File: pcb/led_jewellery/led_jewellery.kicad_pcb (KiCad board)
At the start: 2 copper layers, 12.3 x 27.2 mm, 6 parts, among them J1 Conn_01x01, J2 Conn_01x01, SW1 SW_SPST

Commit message: update pcb
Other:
- board size 12.3 x 27.2 mm -> 12.3 x 25.6 mm
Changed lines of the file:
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@@
 		(grid_origin 124.5 72)
 		(pcbplotparams
-			(layerselection 0x00000000_00000000_55555555_575555ff)
+			(layerselection 0x00000000_00000000_55555555_5755557f)
 			(plot_on_all_layers_selection 0x00000000_00000000_00000000_00000000)
 			(disableapertmacros no)
@@
 			)
 		)
+		(property "LCSC_part#" ""
+			(at 0 0 225)
+			(unlocked yes)
+			(layer "F.Fab")
+			(hide yes)
+			(effects
+				(font
+					(size 1 1)
+					(thickness 0.15)
+				)
+			)
+		)
 		(property ki_fp_filters "LED* LED_SMD:* LED_THT:*")
 		(sheetname "/")
 		(sheetfile "led_jewellery.kicad_sch")
-		(attr smd)
+		(attr smd dnp)
 		(fp_line
 			(start 1.6 1)
@@
 			(at -3.2 0 225)
 			(size 5.5 1)
-			(layers "F.Cu" "F.Mask" "F.Paste")
+			(layers "F.Cu" "F.Mask")
 			(net 3 "/BAT-")
 			(pinfunction "K")
@@
 			(at 3.2 0 225)
 			(size 5.5 1)
-			(layers "F.Cu" "F.Mask" "F.Paste")
+			(layers "F.Cu" "F.Mask")
 			(net 2 "/LED+")
 			(pinfunction "A")
@@
 			)
 		)
+		(property "LCSC_part#" "C17408"
+			(at 0 0 180)
+			(unlocked yes)
+			(layer "F.Fab")
+			(hide yes)
+			(effects
+				(font
+					(size 1 1)
+					(thickness 0.15)
+				)
+			)
+		)
 		(property ki_fp_filters "R_*")
 		(sheetname "/")
@@
 		)
 		(property "Description" "Single Pole Single Throw (SPST) switch"
+			(at 0 0 0)
+			(unlocked yes)
+			(layer "F.Fab")
+			(hide yes)
+			(effects
+				(font
+					(size 1 1)
+					(thickness 0.15)
+				)
+			)
+		)
+		(property "LCSC_part#" "C501583"
 			(at 0 0 0)
 			(unlocked yes)
@@
 			(unlocked yes)
 			(layer "B.SilkS")
+			(hide yes)
 			(effects
 				(font
@@
 		(property "Description" "Generic connector, single row, 01x01, script generated (kicad-library-utils/schlib/autogen/connector/)"
 			(at 0 0 45)
+			(unlocked yes)
+			(layer "B.Fab")
+			(hide yes)
+			(effects
+				(font
+					(size 1 1)
+					(thickness 0.15)
+				)
+				(justify mirror)
+			)
+		)
+		(property "LCSC_part#" ""
+			(at 0 0 225)
 			(unlocked yes)
 			(layer "B.Fab")
@@
 		(sheetname "/")
 		(sheetfile "led_jewellery.kicad_sch")
-		(attr smd)
+		(attr smd dnp)
 		(fp_text user "${REFERENCE}"
 			(at 0 -6.999999 45)
@@
 			(at 0 0 225)
 			(size 9 9)
-			(layers "B.Cu" "B.Mask" "B.Paste")
+			(layers "B.Cu" "B.Mask")
 			(net 3 "/BAT-")
 			(pinfunction "Pin_1")
@@
 			(unlocked yes)
 			(layer "B.SilkS")
+			(hide yes)
 			(effects
 				(font
@@
 		(property "Description" "Generic connector, single row, 01x01, script generated (kicad-library-utils/schlib/autogen/connector/)"
 			(at 0 0 0)
+			(unlocked yes)
+			(layer "B.Fab")
+			(hide yes)
+			(effects
+				(font
+					(size 1 1)
+					(thickness 0.15)
+				)
+				(justify mirror)
+			)
+		)
+		(property "LCSC_part#" ""
+			(at 0 0 180)
 			(unlocked yes)
 			(layer "B.Fab")
@@
 		(sheetname "/")
 		(sheetfile "led_jewellery.kicad_sch")
-		(attr smd)
+		(attr smd dnp)
 		(fp_text user "${REFERENCE}"
 			(at 0 -7 0)
@@
 			(at 0 0 180)
 			(size 9 9)
-			(layers "B.Cu" "B.Mask" "B.Paste")
+			(layers "B.Cu" "B.Mask")
 			(net 4 "/BAT+")
 			(pinfunction "Pin_1")
@@
 	)
 	(gr_arc
-		(start 120.952656 90.468665)
-		(mid 118.826176 90.473825)
-		(end 118.831189 88.347491)
-		(stroke
-			(width 0.05)
-			(type default)
-		)
-		(layer "Edge.Cuts")
-	)
-	(gr_arc
 		(start 127.115338 79.4)
 		(mid 127.339014 79.51417)
@@
 		(layer "Edge.Cuts")
 	)
+	(gr_arc
+		(start 124.5 65.573)
+		(mid 125.304105 65.623501)
+		(end 126.095573 65.774209)
+		(stroke
+			(width 0.05)
+			(type default)
+		)
+		(layer "Edge.Cuts")
+	)
 	(gr_line
 		(start 120.952656 90.468665)
@@
 			(width 0.05)
 			(type solid)
+		)
+		(layer "Edge.Cuts")
+	)
+	(gr_arc
+		(start 122.880439 65.780406)
+		(mid 123.683606 65.625062)
+		(end 124.5 65.573)
+		(stroke
+			(width 0.05)
+			(type default)
+		)
+		(layer "Edge.Cuts")
+	)
+	(gr_arc
+		(start 127.557737 79.637612)
+		(mid 128.742649 80.557367)
+		(end 129.662399 81.742283)
+		(stroke
+			(width 0.05)
+			(type default)
 		)
 		(layer "Edge.Cuts")
@@
 		(layer "Edge.Cuts")
 	)
+	(gr_arc
+		(start 120.952656 90.468665)
+		(mid 119.771517 89.528516)
+		(end 118.83136 88.347384)
+		(stroke
+			(width 0.05)
+			(type default)
+		)
+		(layer "Edge.Cuts")
+	)
 	(gr_line
-		(start 126.111394 65.664411)
-		(end 126.095573 66.222715)
+		(start 126.095571 66.222715)
+		(end 126.095573 65.774209)
+		(stroke
+			(width 0.05)
+			(type default)
+		)
+		(layer "Edge.Cuts")
+	)
+	(gr_line
+		(start 122.880439 66.222717)
+		(end 122.880439 65.780407)
 		(stroke
 			(width 0.05)
@@
 	)
 	(gr_arc
-		(start 122.886016 65.573062)
-		(mid 124.499969 63.959016)
-		(end 126.111394 65.664411)
-		(stroke
-			(width 0.05)
-			(type solid)
-		)
-		(layer "Edge.Cuts")
-	)
-	(gr_arc
 		(start 128.163385 90.289954)
 		(mid 127.289282 90.78163)
@@
 		(stroke
 			(width 0.05)
-			(type default)
-		)
-		(layer "Edge.Cuts")
-	)
-	(gr_arc
-		(start 127.557717 79.637601)
-		(mid 129.803302 79.4967)
-		(end 129.662399 81.742283)
-		(stroke
-			(width 0.05)
-			(type default)
-		)
-		(layer "Edge.Cuts")
-	)
-	(gr_line
-		(start 122.886016 65.573062)
-		(end 122.880439 66.222715)
-		(stroke
-			(width 0.05)

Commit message: first attempt at PCBA layout, x2 boards
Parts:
- added D1: LED, led_jewellery:LED, F.Cu at (117.5, 78.4)
- added J1: Conn_01x01, led_jewellery:9mm_pad, B.Cu at (117.5, 78.4)
- added J2: Conn_01x01, led_jewellery:9mm_pad, B.Cu at (117.5, 91.2)
- added R2: R, Resistor_SMD:R_0805_2012Metric, F.Cu at (121.5, 91.2)
- added SW2: SW_SPST, diptronics_ta3:diptronics_ta3, F.Cu at (115.0, 91.2)
- added mouse-bite-2mm-slot: VAL**, mousebites:mouse-bite-2mm-slot, F.Cu at (111.1, 78.4)
- added mouse-bite-2mm-slot: VAL**, mousebites:mouse-bite-2mm-slot, F.Cu at (111.1, 91.2)
- added mouse-bite-2mm-slot: VAL**, mousebites:mouse-bite-2mm-slot, F.Cu at (106.1, 91.2)
- moved R1 30.6 mm to (95.7, 78.4), turned to -90 degrees
- moved J2 25.6 mm to (99.7, 78.4), turned to -90 degrees
- moved D1 25.6 mm to (99.7, 91.2), turned to 135 degrees
- moved J1 25.6 mm to (99.7, 91.2), turned to 135 degrees
- moved SW1 22.6 mm to (102.2, 78.4), turned to 90 degrees
- moved mouse-bite-2mm-slot 18.4 mm to (106.1, 78.4), turned to 90 degrees
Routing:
- net /BAT+: track 9.06 -> 18.1 mm, vias 4 -> 8
- net /BAT-: track 6.00 -> 12.0 mm, vias 3 -> 6
- net /LED+: track 5.30 -> 10.6 mm, vias 2 -> 4
- net Net-(SW1-B): track 3.34 -> 6.69 mm
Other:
- board size 12.3 x 25.6 mm -> 30.7 x 26.5 mm

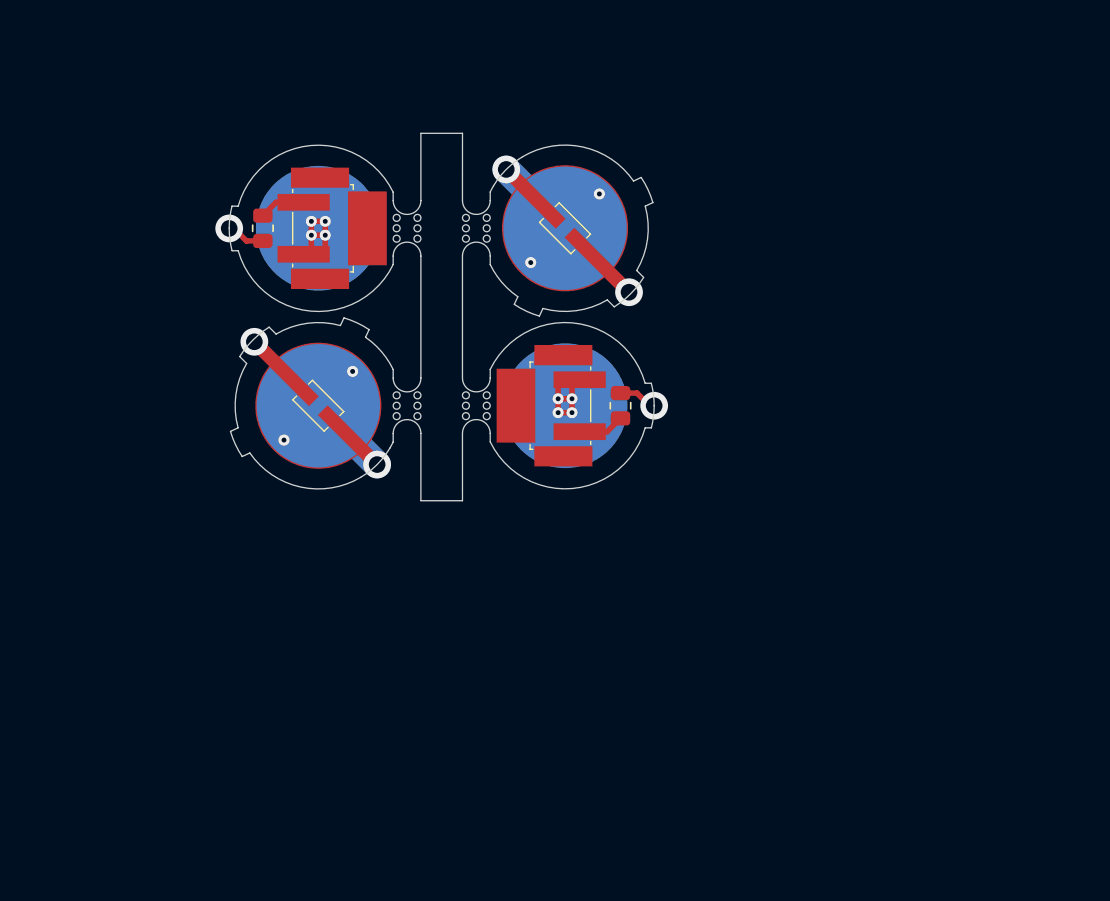
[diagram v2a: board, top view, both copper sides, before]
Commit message: update layout to 6up with larger mousebites
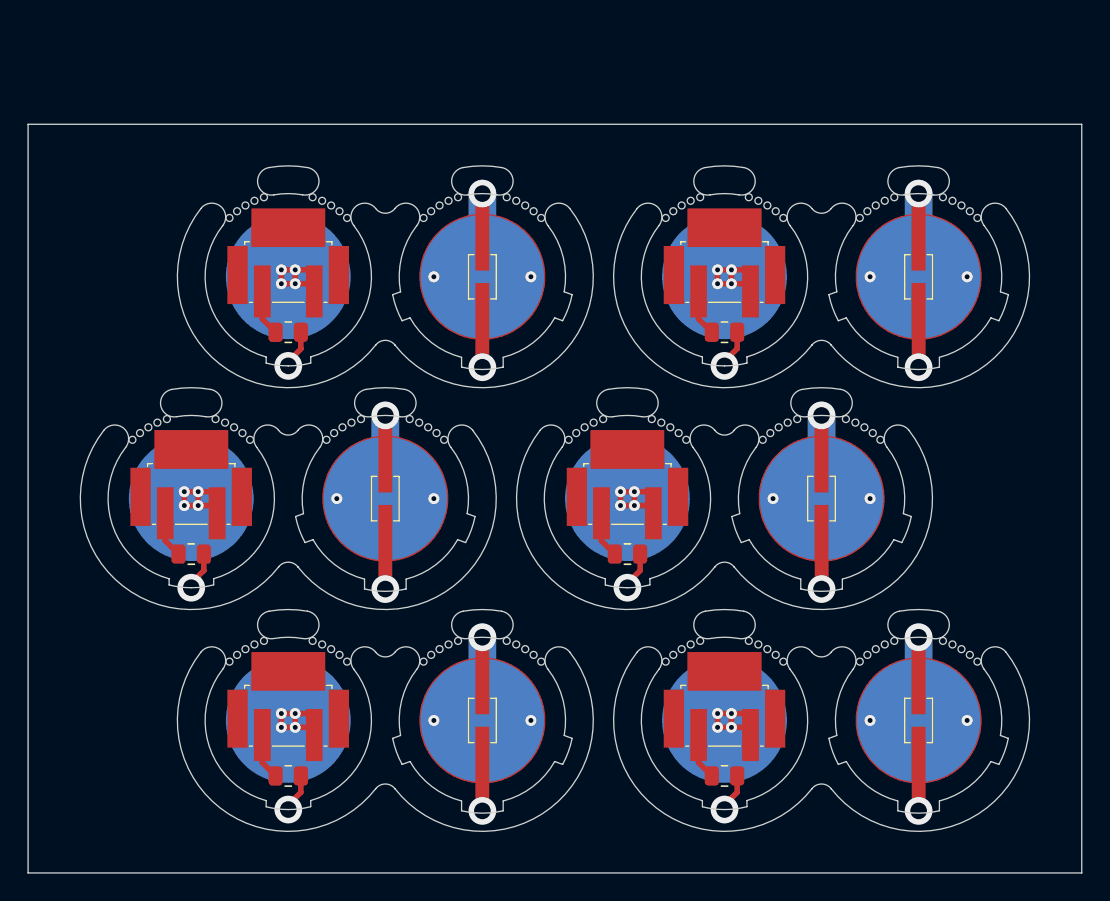
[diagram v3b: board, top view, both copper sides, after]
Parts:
- removed the D1 at (99.7, 91.2)
- removed the J1 at (99.7, 91.2)
- removed the J2 at (99.7, 78.4)
- removed mouse-bite-2mm-slot (x4): VAL**, mousebites:mouse-bite-2mm-slot
- added D1: LED, led_jewellery:LED, F.Cu at (104.5, 97.9)
- added D1: LED, led_jewellery:LED, F.Cu at (143.0, 113.9)
- added D1: LED, led_jewellery:LED, F.Cu at (111.5, 81.9)
- added D1: LED, led_jewellery:LED, F.Cu at (111.5, 113.9)
- added D1: LED, led_jewellery:LED, F.Cu at (143.0, 81.9)
- added J1: Conn_01x01, led_jewellery:9mm_pad, B.Cu at (111.5, 81.9)
- added J1: Conn_01x01, led_jewellery:9mm_pad, B.Cu at (143.0, 113.9)
- added J1: Conn_01x01, led_jewellery:9mm_pad, B.Cu at (111.5, 113.9)
- added J1: Conn_01x01, led_jewellery:9mm_pad, B.Cu at (104.5, 97.9)
- added J1: Conn_01x01, led_jewellery:9mm_pad, B.Cu at (143.0, 81.9)
- added J2: Conn_01x01, led_jewellery:9mm_pad, B.Cu at (129.0, 113.9)
- added J2: Conn_01x01, led_jewellery:9mm_pad, B.Cu at (90.5, 97.9)
- added J2: Conn_01x01, led_jewellery:9mm_pad, B.Cu at (97.5, 81.9)
- added J2: Conn_01x01, led_jewellery:9mm_pad, B.Cu at (97.5, 113.9)
- added J2: Conn_01x01, led_jewellery:9mm_pad, B.Cu at (129.0, 81.9)
- added R2: R, Resistor_SMD:R_0805_2012Metric, F.Cu at (90.5, 101.9)
- added R3: R, Resistor_SMD:R_0805_2012Metric, F.Cu at (97.5, 117.9)
- added R4: R, Resistor_SMD:R_0805_2012Metric, F.Cu at (129.0, 85.9)
- added R6: R, Resistor_SMD:R_0805_2012Metric, F.Cu at (129.0, 117.9)
- added REF** (x2): Untitled, led_jewellery:mousebites_round_12mm, F.Cu at (129.0, 81.9)
- added REF** (x2): Untitled, led_jewellery:mousebites_round_12mm, F.Cu at (129.0, 113.9)
- added REF** (x2): Untitled, led_jewellery:mousebites_round_12mm, F.Cu at (97.5, 113.9)
- added REF** (x2): Untitled, led_jewellery:mousebites_round_12mm, F.Cu at (136.0, 97.9)
- added REF** (x2): Untitled, led_jewellery:mousebites_round_12mm, F.Cu at (104.5, 97.9)
- added REF** (x2): Untitled, led_jewellery:mousebites_round_12mm, F.Cu at (122.0, 97.9)
- added REF** (x2): Untitled, led_jewellery:mousebites_round_12mm, F.Cu at (111.5, 113.9)
- added REF** (x2): Untitled, led_jewellery:mousebites_round_12mm, F.Cu at (90.5, 97.9)
- added REF** (x2): Untitled, led_jewellery:mousebites_round_12mm, F.Cu at (97.5, 81.9)
- added REF** (x2): Untitled, led_jewellery:mousebites_round_12mm, F.Cu at (111.5, 81.9)
- added REF** (x2): Untitled, led_jewellery:mousebites_round_12mm, F.Cu at (143.0, 81.9)
- added REF** (x2): Untitled, led_jewellery:mousebites_round_12mm, F.Cu at (143.0, 113.9)
- added SW2: SW_SPST, diptronics_ta3:diptronics_ta3, F.Cu at (90.5, 97.8)
- added SW3: SW_SPST, diptronics_ta3:diptronics_ta3, F.Cu at (97.5, 113.8)
- added SW4: SW_SPST, diptronics_ta3:diptronics_ta3, F.Cu at (129.0, 81.8)
- added SW6: SW_SPST, diptronics_ta3:diptronics_ta3, F.Cu at (129.0, 113.8)
- moved D1 26.9 mm to (136.0, 97.9), turned to -90 degrees
- moved J1 26.9 mm to (136.0, 97.9), turned to -90 degrees
- moved R5 10.7 mm to (122.0, 101.9), turned to 0 degrees
- moved SW5 9.62 mm to (122.0, 97.8), turned to 180 degrees
- moved J2 8.07 mm to (122.0, 97.9), turned to 0 degrees
- moved R1 7.72 mm to (97.5, 85.9), turned to 0 degrees
- moved SW1 5.78 mm to (97.5, 81.8), turned to 180 degrees
- renumbered R2 to R5, SW2 to SW5
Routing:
- net /BAT+: track 18.1 -> 54.4 mm, vias 8 -> 24
- net /BAT-: track 12.0 -> 36.0 mm, vias 6 -> 18
- net /LED+: track 10.6 -> 31.8 mm, vias 4 -> 12
- net Net-(SW1-B): track 6.69 -> 20.1 mm
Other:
- board size 30.7 x 26.5 mm -> 76 x 54 mm
